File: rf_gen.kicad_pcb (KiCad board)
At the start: 2 copper layers, 40 parts, among them J1 Conn_01x07_Male, J2 Conn_01x02_Female, J3 Conn_01x05_Male, J4 Jack-DC, Q1 GS61004B, Q2 G3R350MT12J, U1 NPC81074, U2 AP62150

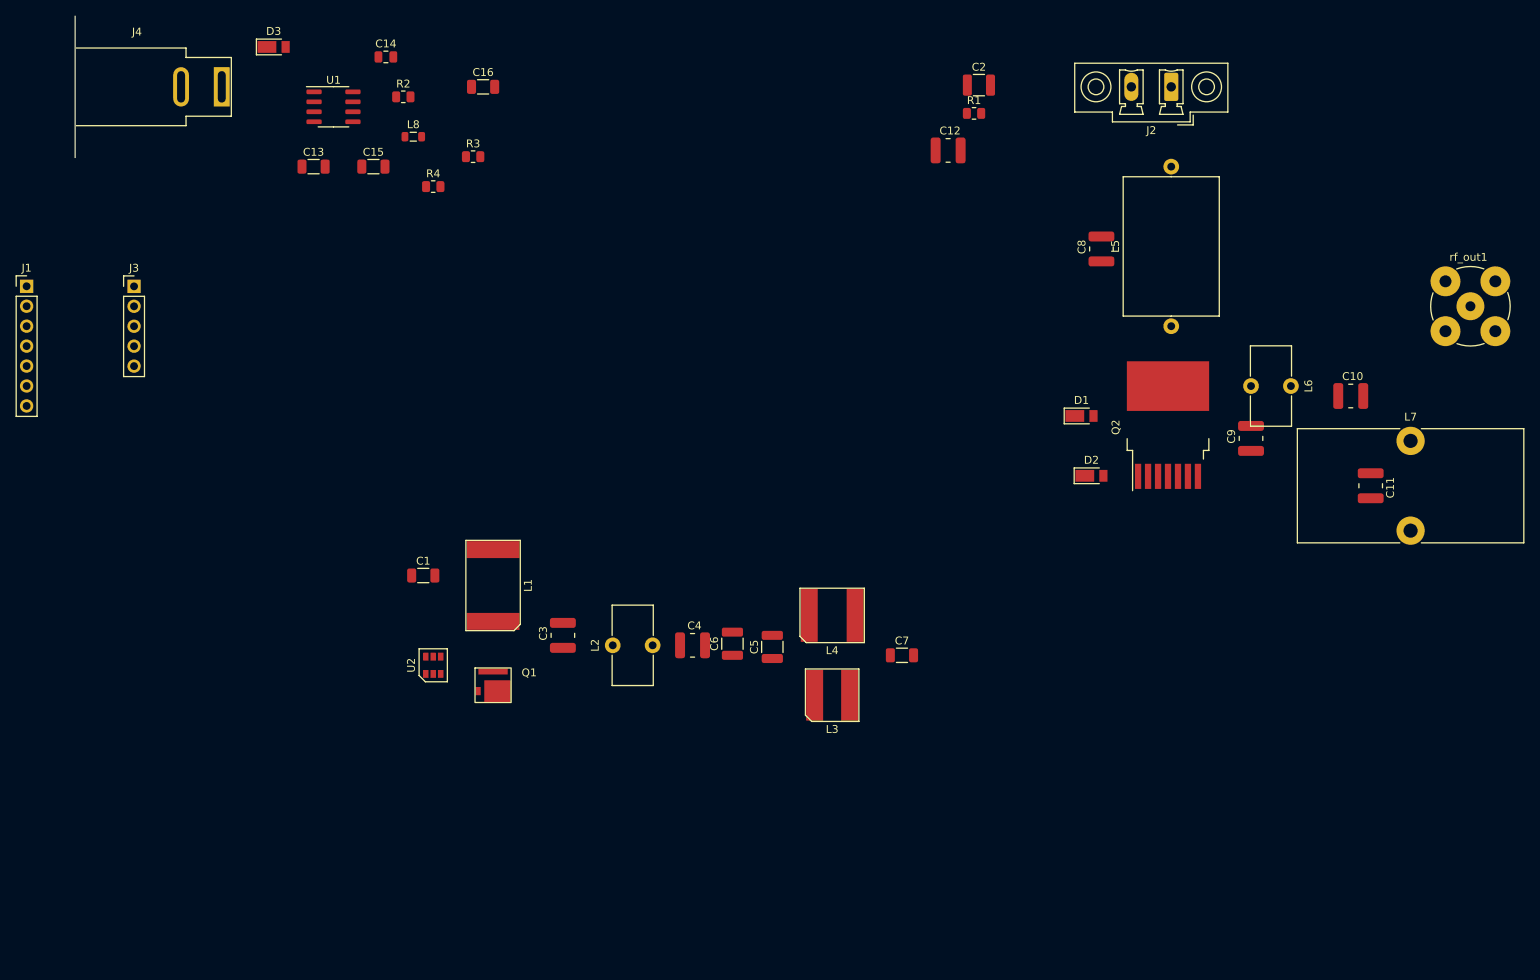
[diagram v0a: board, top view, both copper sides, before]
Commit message: First draft of PCB layout
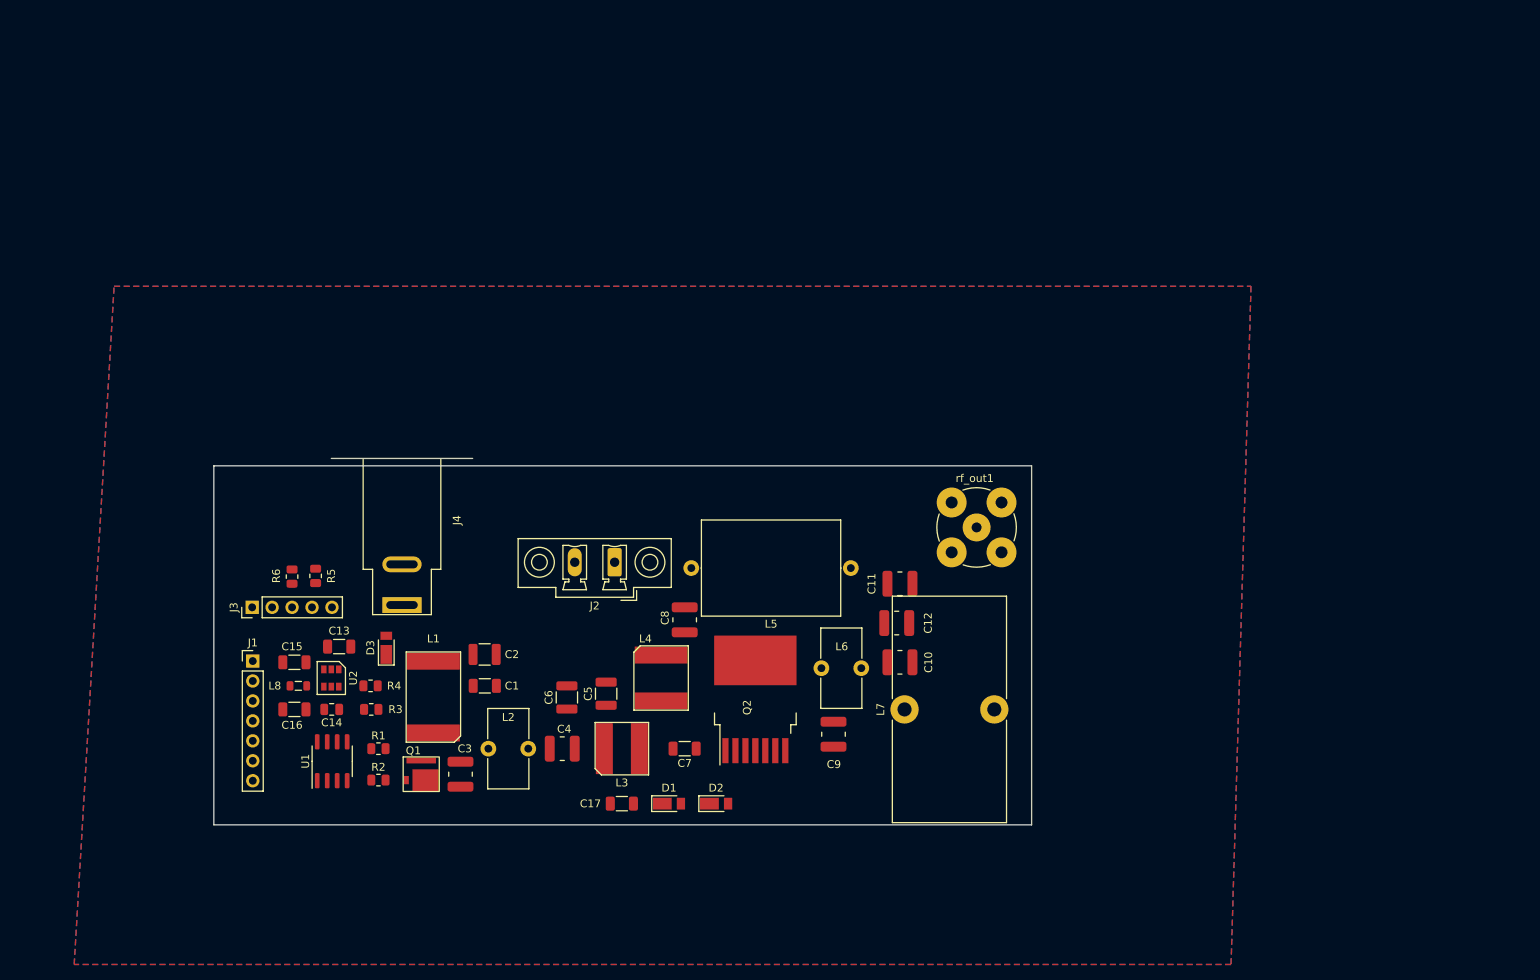
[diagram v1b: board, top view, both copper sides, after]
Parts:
- added C17: 100n, Capacitor_SMD:C_1206_3216Metric, F.Cu at (118.0, 137.0)
- added R5: 10k, Resistor_SMD:R_0805_2012Metric, F.Cu at (79.0, 108.0)
- added R6: 10k, Resistor_SMD:R_0805_2012Metric, F.Cu at (76.0, 108.1)
- moved R1 110.9 mm to (87.0, 130.0)
- moved C2 96.0 mm to (100.5, 118.0), turned to 180 degrees
- moved J2 93.2 mm to (117.1, 106.3)
- moved R2 87.1 mm to (87.0, 134.0)
- moved C14 83.4 mm to (81.0, 125.0), turned to 180 degrees
- moved U1 83.3 mm to (81.1, 131.6), turned to 90 degrees
- moved C16 82.8 mm to (76.3, 125.0)
- moved D3 77.8 mm to (88.0, 117.2), turned to 90 degrees
- moved L7 73.0 mm to (154.0, 125.0), turned to 90 degrees
- moved D1 72.1 mm to (124.0, 137.0)
- moved R3 71.6 mm to (86.1, 125.0)
- moved L8 71.4 mm to (76.8, 122.0), turned to 180 degrees
- moved C8 71.0 mm to (126.0, 113.6)
- moved J4 69.9 mm to (90.0, 111.7), turned to -90 degrees
- moved rf_out1 68.9 mm to (163.2, 101.8)
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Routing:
- added copper zone on B.Cu, net GND
- added copper zone on F.Cu, net GND
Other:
- board outline added: 104.1 x 45.7 mm

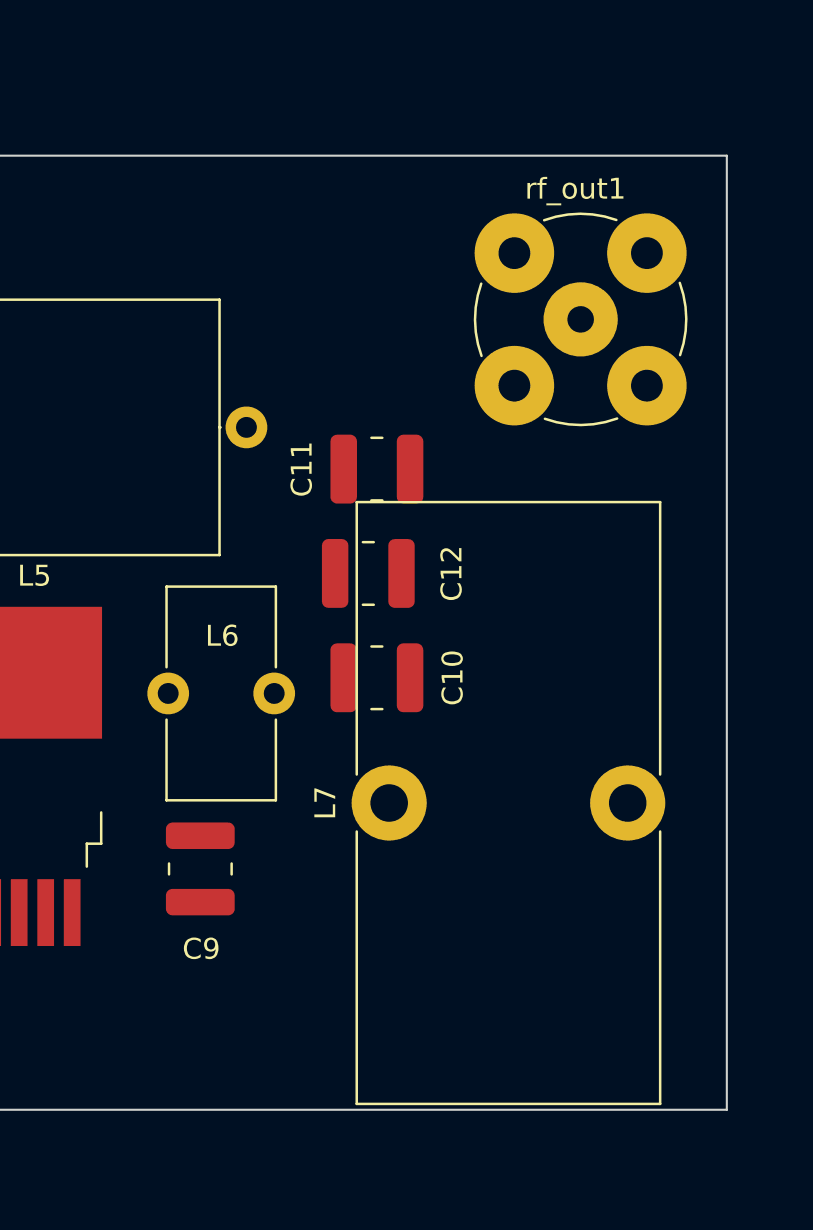
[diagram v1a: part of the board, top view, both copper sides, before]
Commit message: Added simulation and design notes
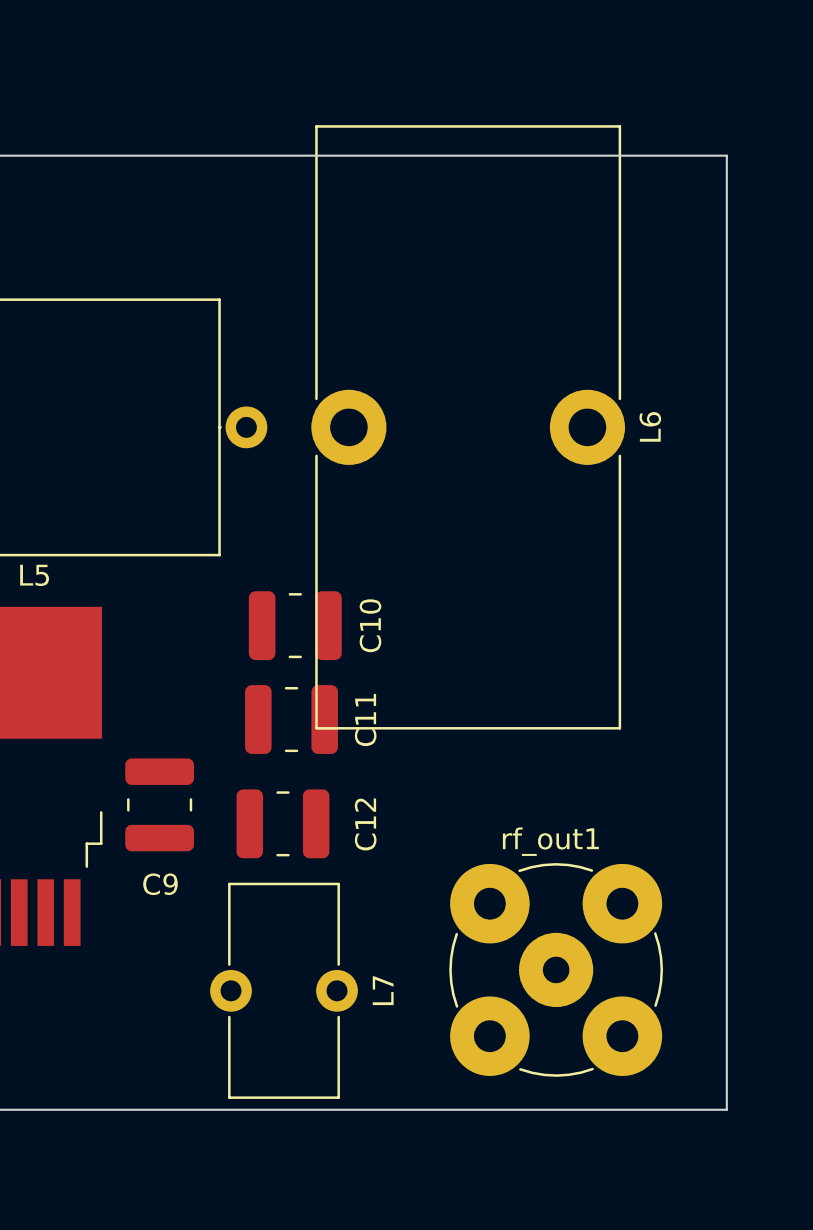
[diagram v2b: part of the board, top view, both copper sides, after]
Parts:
- L6: footprint Inductor_THT:L_Toroid_Vertical_L10.0mm_W5.0mm_P5.08mm -> Inductor_THT:L_Toroid_Vertical_L28.6mm_W14.3mm_P11.43mm_Bourns_5700
- L7: footprint Inductor_THT:L_Toroid_Vertical_L28.6mm_W14.3mm_P11.43mm_Bourns_5700 -> Inductor_THT:L_Toroid_Vertical_L10.0mm_W5.0mm_P5.08mm
- moved rf_out1 31.2 mm to (162.0, 133.0)
- moved L6 19.7 mm to (163.5, 107.0)
- moved C11 12.7 mm to (149.3, 121.0)
- moved C12 12.7 mm to (148.9, 126.0)
- moved L7 9.34 mm to (151.5, 134.0), turned to -90 degrees
- moved C10 4.64 mm to (149.5, 116.5)
- moved C9 3.64 mm to (143.0, 125.1)

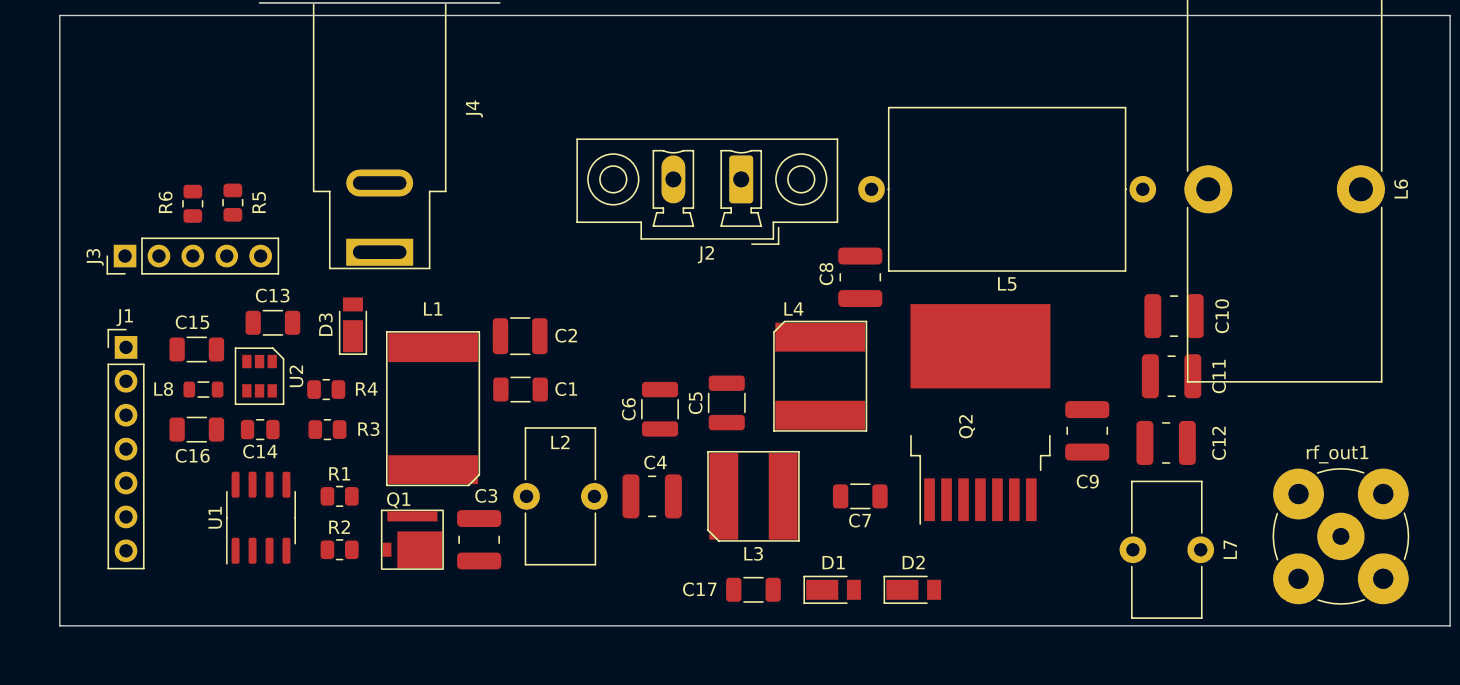
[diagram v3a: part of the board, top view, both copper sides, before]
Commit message: Draft of trace routing
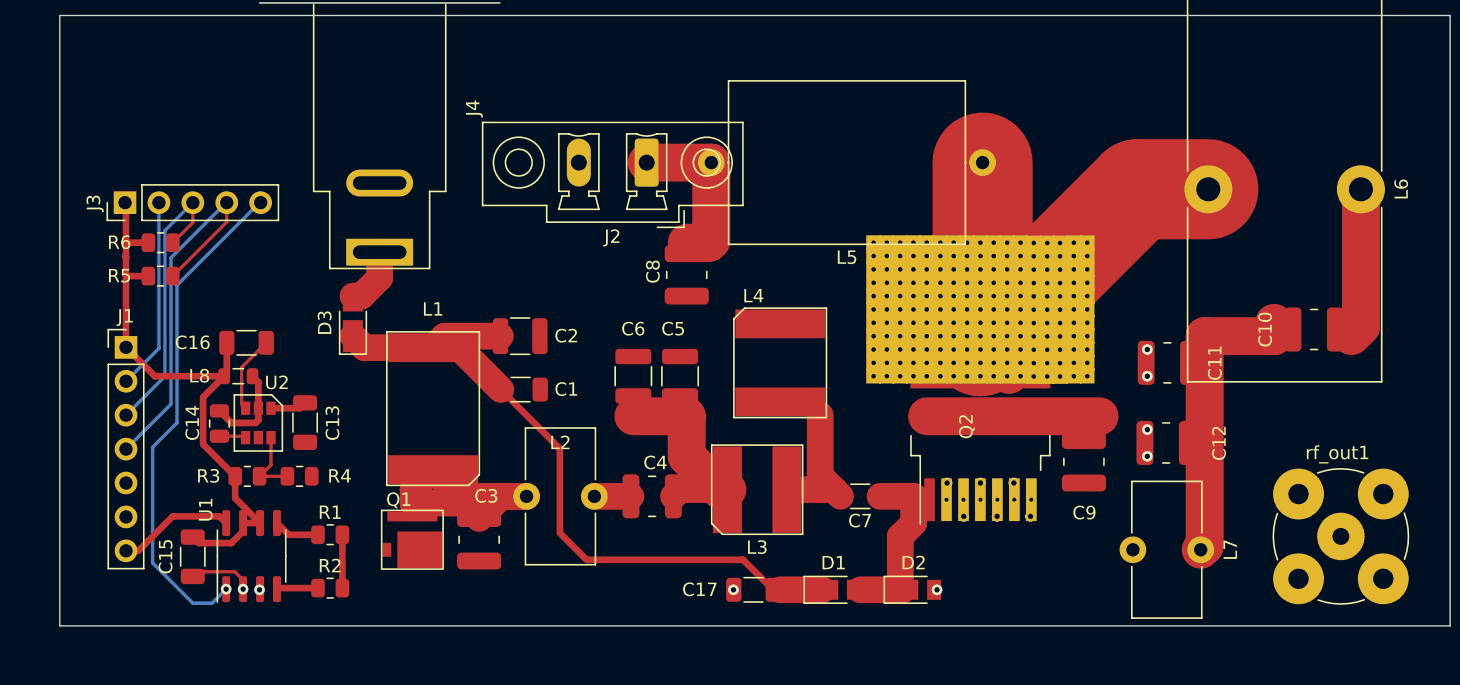
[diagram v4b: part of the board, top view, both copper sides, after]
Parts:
- Q2: footprint rf_gen:TO-263-7_nmos -> rf_gen:TO-263-7_heatsink
- moved C15 15.5 mm to (76.0, 134.5), turned to -90 degrees
- moved C8 13.0 mm to (113.0, 113.4)
- moved L5 12.2 mm to (135.2, 105.0)
- moved C10 10.5 mm to (160.0, 117.5), turned to 180 degrees
- moved C13 7.85 mm to (84.4, 124.5), turned to -90 degrees
- moved R5 7.72 mm to (73.6, 113.5), turned to 180 degrees
- moved C16 7.49 mm to (80.0, 118.5)
- moved J2 7.19 mm to (110.0, 105.0)
- moved R3 6.95 mm to (80.1, 128.5)
- moved R4 6.80 mm to (84.0, 128.5)
- moved C5 4.03 mm to (112.5, 121.0)
- moved J3 4.00 mm to (70.9, 108.0)
- moved R6 3.78 mm to (73.6, 111.0), turned to 0 degrees
- moved U2 3.50 mm to (80.9, 124.5)
- moved C6 3.18 mm to (109.0, 121.0)
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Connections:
- R3 pad 1: Net-(C14-Pad2) -> +5V
- rf_out1 pad 2: unconnected-(rf_out1-Pad2) -> GND
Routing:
- net +12V: track 0.00 -> 54.3 mm
- net Net-(C9-Pad2): track 0.00 -> 48.0 mm
- net +5V: track 0.00 -> 44.8 mm
- net /EN: track 0.00 -> 37.6 mm, vias 0 -> 1
- net /SCL: track 0.00 -> 28.8 mm
- net GND: track 0.00 -> 25.0 mm, vias 0 -> 14
- net Net-(C10-Pad2): track 0.00 -> 22.3 mm
- net Net-(C3-Pad2): track 0.00 -> 22.0 mm
- net /SDA: track 0.00 -> 21.6 mm
- net Net-(C4-Pad2): track 0.00 -> 15.3 mm
- net /SiC_gate: track 0.00 -> 13.2 mm
- net VDD: track 0.00 -> 12.6 mm
- net Net-(C10-Pad1): track 0.00 -> 11.3 mm
- net Net-(C7-Pad2): track 0.00 -> 10.2 mm
- net /13.56Mhz: track 0.00 -> 8.78 mm
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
